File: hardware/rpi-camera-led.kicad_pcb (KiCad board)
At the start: 2 copper layers, 25 x 23.9 mm, 20 parts, among them J1 FFC 15P 1.0mm bottom contact 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, J2 FFC 15P 1.0mm top contact (to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, J3 Qwiic (JST SH 1.0mm), J4 SWD program header 2.54mm, Q1 AO3400A, Q2 Phototransistor, U1 CH32V003A4M6

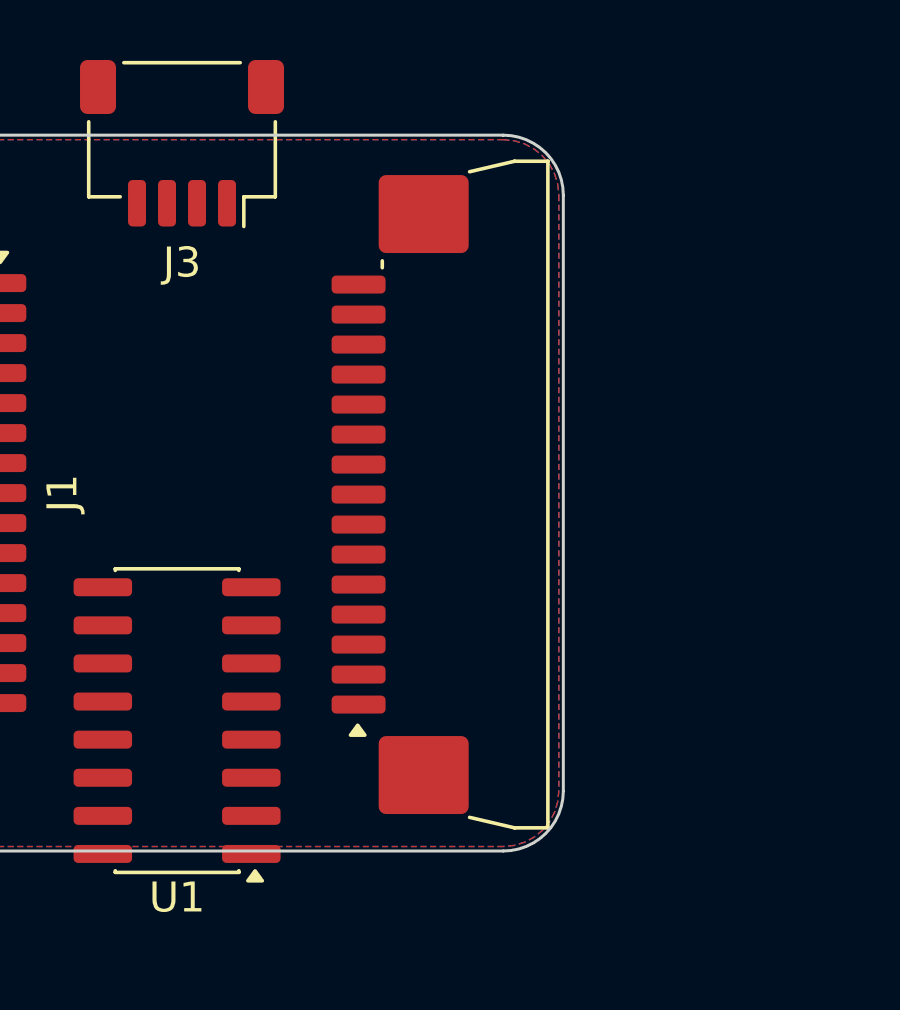
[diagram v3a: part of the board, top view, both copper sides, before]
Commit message: Place J2 as an exact mirror of J1
The two connectors were not identically placed: J1's pad column sat
6.300mm left of the board centre and J2's only 5.675mm right, with the
rows a further 0.049mm apart in Y.  Every pass-through net would have
needed a small dogleg at one end, which is a silly way to spend a
straight bus.

J2 goes back to (42.175, 31.931), where it was in 351c3b2 before the
interrupted session nudged it to (41.55, 31.98).  That is J1 mirrored
about the board's vertical centreline:

    pad column      J1 x=26.200        J2 x=38.800
    from centre     6.300mm            6.300mm
    mounting pads   (24.03, 22.581)    (40.97, 22.581)
                    (24.03, 41.281)    (40.97, 41.281)

Measured after the move, the worst |dY| over all fifteen facing pairs
J1.k / J2.(16-k) is 0.000000mm, so each pass-through net is now a
straight horizontal run of 12.6mm at constant Y.

DRC goes 92 -> 93 and schematic parity stays 0.  The delta is itself a
symptom of the symmetry: silk_edge_clearance 4 -> 6, because J2 now
sits where its silkscreen is clipped by the rounded corner exactly as
J1's already was, and starved_thermal 5 rather than 6.  The connector
silkscreen overhanging the board corners is worth cleaning up, but it
affects both ends equally now.

Co-Authored-By: Claude Opus 5 (1M context) <noreply@anthropic.com>
Claude-Session: https://claude.ai/code/session_01E6VQHygrbAGSqdngQQsBdx
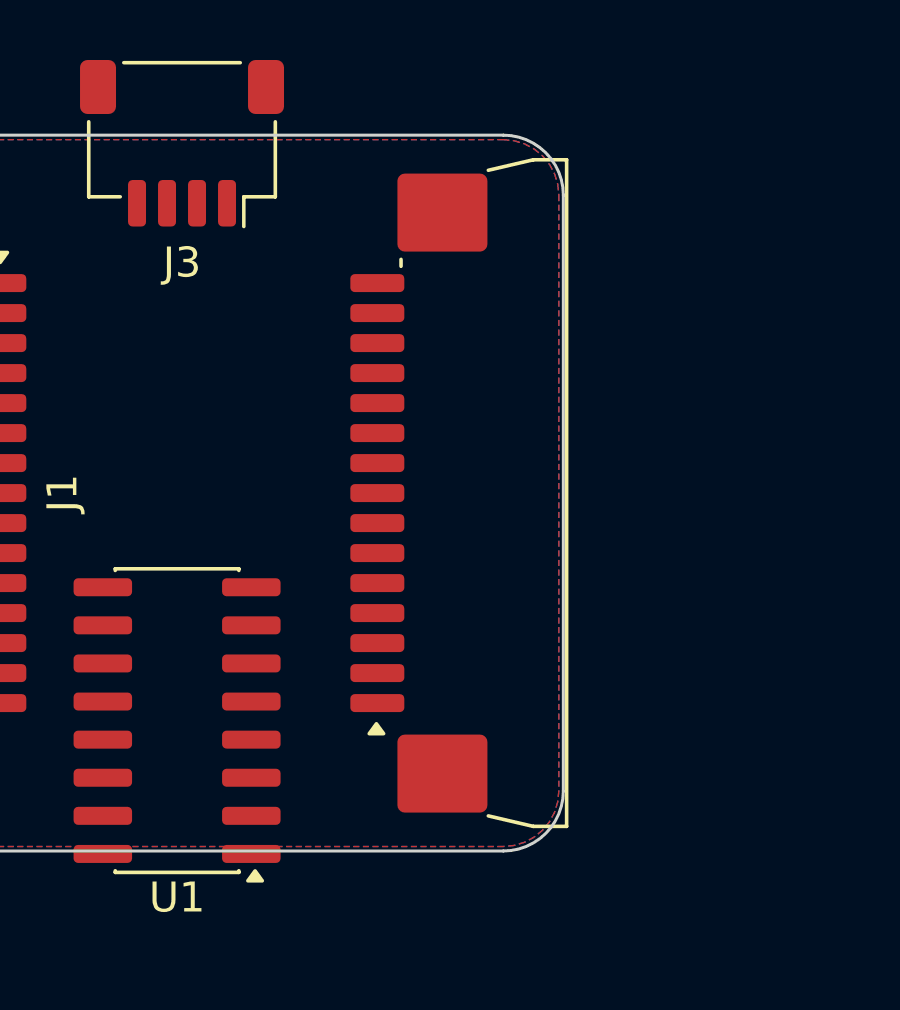
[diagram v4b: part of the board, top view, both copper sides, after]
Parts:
- moved J2 0.63 mm to (42.2, 31.9)
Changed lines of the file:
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@@
 	(footprint "rpi-camera-led:JUSHUO_AFA07-S15ECA-00_1x15-1MP_P1.0mm_Horizontal"
 		(layer "F.Cu")
-		(at 41.55 31.98 90)
+		(at 42.175 31.931 90)
 		(descr "JUSHUO FPC connector, 15 TOP-side contacts, 1.0mm pitch, 2.5mm height, SMT. Same land pattern as the bottom-contact AFA07-S15FCA-00 (identical recommended PCB pattern in the shared AFA07 series drawing); only the contact side differs, so the cable inserts flipped. https://www.lcsc.com/datasheet/lcsc_datasheet_2304140030_JUSHUO-AFA07-S15ECA-00_C262742.pdf")
 		(tags "jushuo fpc top contact")

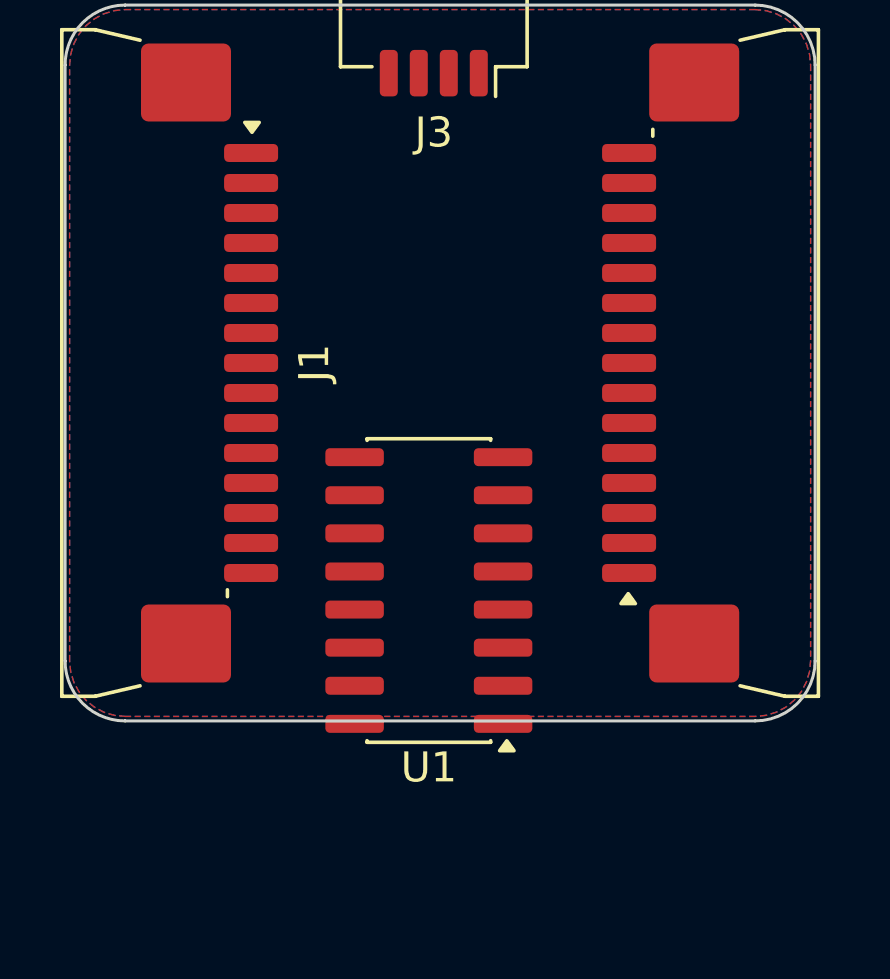
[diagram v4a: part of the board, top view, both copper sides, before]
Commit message: Tim's KiCad session: six straight MIPI runs, J2 re-mirrored
Committing the working files as they stand so the routing is not lost.
This is an inconsistent intermediate state, recorded rather than
tidied, because the two halves disagree:

  * Six straight traces on F.Cu, 0.2mm, each a full 12.6mm run at
    constant Y from J1's pad column to J2's -- the MIPI pairs and
    clock, exactly the payoff the alignment work was for.
  * J2 carries (mirror x) again, which puts the connector mapping back
    to J1.k <-> J2.k and undoes be3c223.

Straight runs need the reversed mapping, so with the mirror back five
of the six traces land on a pad of the wrong net: CAM_CK_P on J2.7
(GND), CAM_D0_N on J2.14 (SDA), CAM_D0_P on J2.13 (SCL), CAM_D1_N on
J2.11 (CAM_IO0), CAM_D1_P on J2.10 (GND).  Only CAM_CK_N is right, pin
8 being the one pin where both mappings agree.  Hence DRC 93 -> 111 and
one net fewer unconnected.

Everything else from the recent commits survived the save, so this
looks like the schematic editor writing back a buffer loaded before
be3c223 rather than a decision.

Co-Authored-By: Claude Opus 5 (1M context) <noreply@anthropic.com>
Claude-Session: https://claude.ai/code/session_01E6VQHygrbAGSqdngQQsBdx
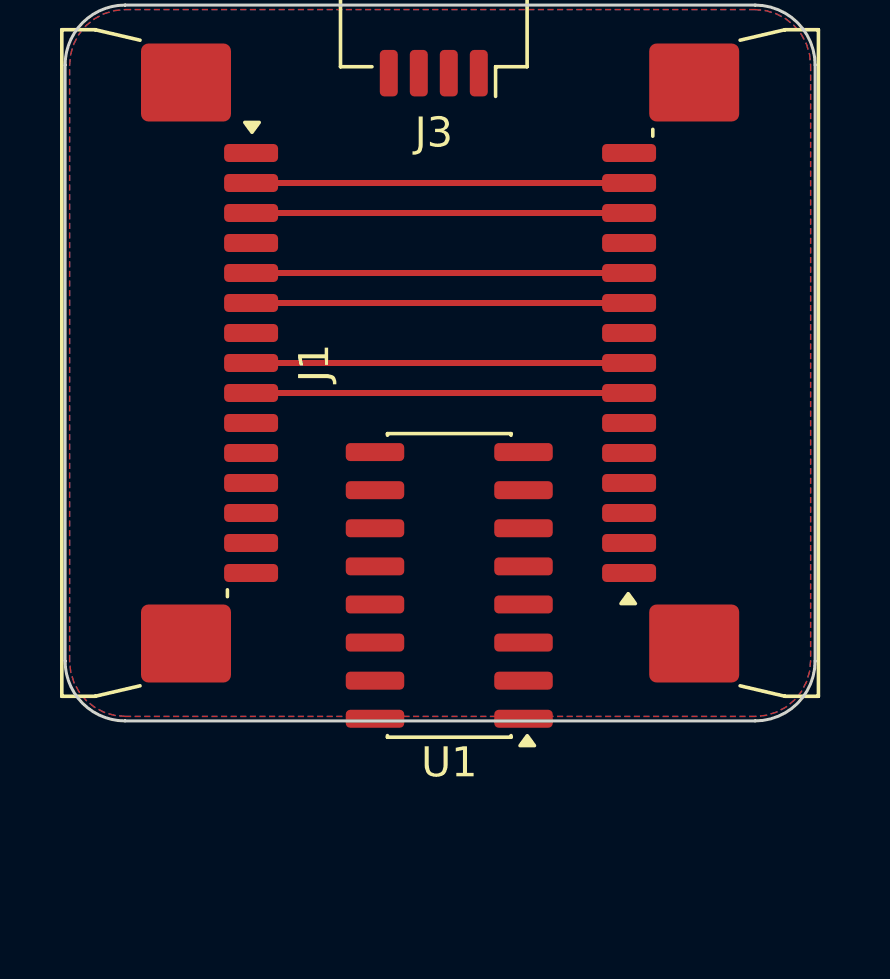
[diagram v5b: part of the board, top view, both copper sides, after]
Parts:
- moved U1 0.70 mm to (32.8, 39.3)
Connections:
- J2 pad 1: 3V3 -> GND
- J2 pad 10: CAM_D1_P -> GND
- J2 pad 11: CAM_D1_N -> CAM_IO0
- J2 pad 12: GND -> CAM_IO1
- J2 pad 13: CAM_D0_P -> SCL
- J2 pad 14: CAM_D0_N -> SDA
- J2 pad 15: GND -> 3V3
- J2 pad 2: SDA -> CAM_D0_N
- J2 pad 3: SCL -> CAM_D0_P
- J2 pad 4: CAM_IO1 -> GND
- J2 pad 5: CAM_IO0 -> CAM_D1_N
- J2 pad 6: GND -> CAM_D1_P
- J2 pad 7: CAM_CK_P -> GND
- J2 pad 9: GND -> CAM_CK_P
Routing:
- net CAM_D1_P: track 0.00 -> 12.6 mm
- net CAM_D1_N: track 0.00 -> 12.6 mm
- net CAM_D0_P: track 0.00 -> 12.6 mm
- net CAM_D0_N: track 0.00 -> 12.6 mm
- net CAM_CK_P: track 0.00 -> 12.6 mm
- net CAM_CK_N: track 0.00 -> 12.6 mm
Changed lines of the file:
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@@
 			(layers "F.Cu" "F.Mask" "F.Paste")
 			(roundrect_rratio 0.25)
-			(net 1 "3V3")
+			(net 10 "GND")
 			(pinfunction "Pin_1")
 			(pintype "passive")
@@
 			(layers "F.Cu" "F.Mask" "F.Paste")
 			(roundrect_rratio 0.25)
-			(net 19 "SDA")
+			(net 4 "CAM_D0_N")
 			(pinfunction "Pin_2")
 			(pintype "passive")
@@
 			(layers "F.Cu" "F.Mask" "F.Paste")
 			(roundrect_rratio 0.25)
-			(net 18 "SCL")
+			(net 5 "CAM_D0_P")
 			(pinfunction "Pin_3")
 			(pintype "passive")
@@
 			(layers "F.Cu" "F.Mask" "F.Paste")
 			(roundrect_rratio 0.25)
-			(net 9 "CAM_IO1")
+			(net 10 "GND")
 			(pinfunction "Pin_4")
 			(pintype "passive")
@@
 			(layers "F.Cu" "F.Mask" "F.Paste")
 			(roundrect_rratio 0.25)
-			(net 8 "CAM_IO0")
+			(net 6 "CAM_D1_N")
 			(pinfunction "Pin_5")
 			(pintype "passive")
@@
 			(layers "F.Cu" "F.Mask" "F.Paste")
 			(roundrect_rratio 0.25)
-			(net 10 "GND")
+			(net 7 "CAM_D1_P")
 			(pinfunction "Pin_6")
 			(pintype "passive")
@@
 			(layers "F.Cu" "F.Mask" "F.Paste")
 			(roundrect_rratio 0.25)
-			(net 3 "CAM_CK_P")
+			(net 10 "GND")
 			(pinfunction "Pin_7")
 			(pintype "passive")
@@
 			(layers "F.Cu" "F.Mask" "F.Paste")
 			(roundrect_rratio 0.25)
-			(net 10 "GND")
+			(net 3 "CAM_CK_P")
 			(pinfunction "Pin_9")
 			(pintype "passive")
@@
 			(layers "F.Cu" "F.Mask" "F.Paste")
 			(roundrect_rratio 0.25)
-			(net 7 "CAM_D1_P")
+			(net 10 "GND")
 			(pinfunction "Pin_10")
 			(pintype "passive")
@@
 			(layers "F.Cu" "F.Mask" "F.Paste")
 			(roundrect_rratio 0.25)
-			(net 6 "CAM_D1_N")
+			(net 8 "CAM_IO0")
 			(pinfunction "Pin_11")
 			(pintype "passive")
@@
 			(layers "F.Cu" "F.Mask" "F.Paste")
 			(roundrect_rratio 0.25)
-			(net 10 "GND")
+			(net 9 "CAM_IO1")
 			(pinfunction "Pin_12")
 			(pintype "passive")
@@
 			(layers "F.Cu" "F.Mask" "F.Paste")
 			(roundrect_rratio 0.25)
-			(net 5 "CAM_D0_P")
+			(net 18 "SCL")
 			(pinfunction "Pin_13")
 			(pintype "passive")
@@
 			(layers "F.Cu" "F.Mask" "F.Paste")
 			(roundrect_rratio 0.25)
-			(net 4 "CAM_D0_N")
+			(net 19 "SDA")
 			(pinfunction "Pin_14")
 			(pintype "passive")
@@
 			(layers "F.Cu" "F.Mask" "F.Paste")
 			(roundrect_rratio 0.25)
-			(net 10 "GND")
+			(net 1 "3V3")
 			(pinfunction "Pin_15")
 			(pintype "passive")
@@
 	(footprint "Package_SO:SOIC-16_3.9x9.9mm_P1.27mm"
 		(layer "F.Cu")
-		(at 32.125 39.515 180)
+		(at 32.805 39.345 180)
 		(descr "SOIC, 16 Pin (JEDEC MS-012, variation AC, https://www.jedec.org/document_search?search_api_views_fulltext=MS-012, https://www.analog.com/media/en/package-pcb-resources/package/pkg_pdf/soic_narrow-r/r_16.pdf), generated with kicad-footprint-generator ipc_gullwing_generator.py")
 		(tags "SOIC SO 16-pin-NSOP R-16 R-16-S D0016A M2B SO16 SOT109-1 751B SOIC_N narrow")
@@
 		(layer "Edge.Cuts")
 	)
+	(segment
+		(start 38.8 31.931)
+		(end 26.2 31.931)
+		(width 0.2)
+		(layer "F.Cu")
+		(net 2)
+	)
+	(segment
+		(start 38.8 32.931)
+		(end 26.2 32.931)
+		(width 0.2)
+		(layer "F.Cu")
+		(net 3)
+	)
+	(segment
+		(start 38.8 25.931)
+		(end 26.2 25.931)
+		(width 0.2)
+		(layer "F.Cu")
+		(net 4)
+	)
+	(segment
+		(start 26.2 26.931)
+		(end 38.8 26.931)
+		(width 0.2)
+		(layer "F.Cu")
+		(net 5)
+	)
+	(segment
+		(start 38.8 28.931)
+		(end 26.2 28.931)
+		(width 0.2)
+		(layer "F.Cu")
+		(net 6)
+	)
+	(segment
+		(start 38.8 29.931)
+		(end 26.2 29.931)
+		(width 0.2)
+		(layer "F.Cu")
+		(net 7)
+	)
 	(zone

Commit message: Put J2 back on the original bottom-contact part
Undo a708eef and be3c223: J1 and J2 are the same AFA07-S15FCA-00
again, wired pin-for-pin, so a standard same-side Raspberry Pi camera
cable works at both ends.  That was the real cost of the top-contact
route -- it needed an opposite-side (type D) FFC or a fold on the
camera segment, which is a poor trade for a board whose point is to sit
transparently in an existing cable run.

Everything that existed only to support the swap goes with it: the
project footprint library holding the renamed ECA copy, its
fp-lib-table, the contact-type annotations in both connectors' Value
and MPN fields, and the on-sheet note explaining why the parts
differed.  The board's embedded copy of the footprint goes back to the
stock KiCad one, pads asserted unchanged.

check_schematic.py drops the pass-through invariant, which is not
satisfiable now and would only nag: pin k is wired to pin k but faces
pin 16-k, so the bus cannot be fifteen straight traces.  Its expected
nets follow J2's pins back to the straight mapping.  check_pcb.py keeps
the facing-alignment measurement, which is still worth having -- it is
what catches a connector drifting out of mirror.

Still broken and left alone deliberately: five of the six traces in
fdd04d9 land on a pad of the wrong net, because straight runs only work
under the reversed mapping.  DRC stays at 111 violations, 49
unconnected.  They want deleting before the bus is re-routed, which is
a call for Tim rather than something to tidy away.

Co-Authored-By: Claude Opus 5 (1M context) <noreply@anthropic.com>
Claude-Session: https://claude.ai/code/session_01E6VQHygrbAGSqdngQQsBdx
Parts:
- J1: value FFC 15P 1.0mm bottom contact (to Raspberry Pi) -> FFC 15P 1.0mm (to Raspberry Pi)
- J2: value FFC 15P 1.0mm top contact (to camera) -> FFC 15P 1.0mm (to camera); footprint rpi-camera-led:JUSHUO_AFA07-S15ECA-00_1x15-1MP_P1.0mm_Horizontal -> Connector_FFC-FPC:JUSHUO_AFA07-S15FCA-00_1x15-1MP_P1.0mm_Horizontal
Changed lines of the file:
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@@
 			)
 		)
-		(property "Value" "FFC 15P 1.0mm bottom contact (to Raspberry Pi)"
+		(property "Value" "FFC 15P 1.0mm (to Raspberry Pi)"
 			(at 0 5.68 270)
 			(layer "F.Fab")
@@
 			)
 		)
-		(property "MPN" "JUSHUO AFA07-S15FCA-00 (bottom contact, LCSC C262721)"
+		(property "MPN" "JUSHUO AFA07-S15FCA-00 / Amphenol SFW15R-1STE1LF"
 			(at 0 0 270)
 			(unlocked yes)
@@
 		)
 	)
-	(footprint "rpi-camera-led:JUSHUO_AFA07-S15ECA-00_1x15-1MP_P1.0mm_Horizontal"
+	(footprint "Connector_FFC-FPC:JUSHUO_AFA07-S15FCA-00_1x15-1MP_P1.0mm_Horizontal"
 		(layer "F.Cu")
 		(at 42.175 31.931 90)
-		(descr "JUSHUO FPC connector, 15 TOP-side contacts, 1.0mm pitch, 2.5mm height, SMT. Same land pattern as the bottom-contact AFA07-S15FCA-00 (identical recommended PCB pattern in the shared AFA07 series drawing); only the contact side differs, so the cable inserts flipped. https://www.lcsc.com/datasheet/lcsc_datasheet_2304140030_JUSHUO-AFA07-S15ECA-00_C262742.pdf")
-		(tags "jushuo fpc top contact")
+		(descr "JUSHUO FPC connector, 15 bottom-side contacts, 1.0mm pitch, 2.5mm height, SMT, https://www.lcsc.com/datasheet/lcsc_datasheet_2304140030_JUSHUO-AFA07-S04FCA-00_C262710.pdf")
+		(tags "jushuo fpc")
 		(property "Reference" "J2"
 			(at 0 -5.48 90)
@@
 			)
 		)
-		(property "Value" "FFC 15P 1.0mm top contact (to camera)"
+		(property "Value" "FFC 15P 1.0mm (to camera)"
 			(at 0 5.68 90)
 			(layer "F.Fab")
@@
 			)
 		)
-		(property "MPN" "JUSHUO AFA07-S15ECA-00 (top contact, LCSC C262742)"
+		(property "MPN" "JUSHUO AFA07-S15FCA-00 / Amphenol SFW15R-1STE1LF"
 			(at 0 0 90)
 			(unlocked yes)
